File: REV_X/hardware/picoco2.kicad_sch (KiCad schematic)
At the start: 40 parts, among them J1 Conn_01x03_Female, J2 Micro_SD_Card, J3 Conn_01x03_Female, Q1 Q_NMOS_GDS, SW1 SW_Push, SW2 SW_Push, U1 PicoW, U2 scd30, U3 ssd1306, U4 PCF8523T, U5 MCP73831-2-OT, Y1 32KHz

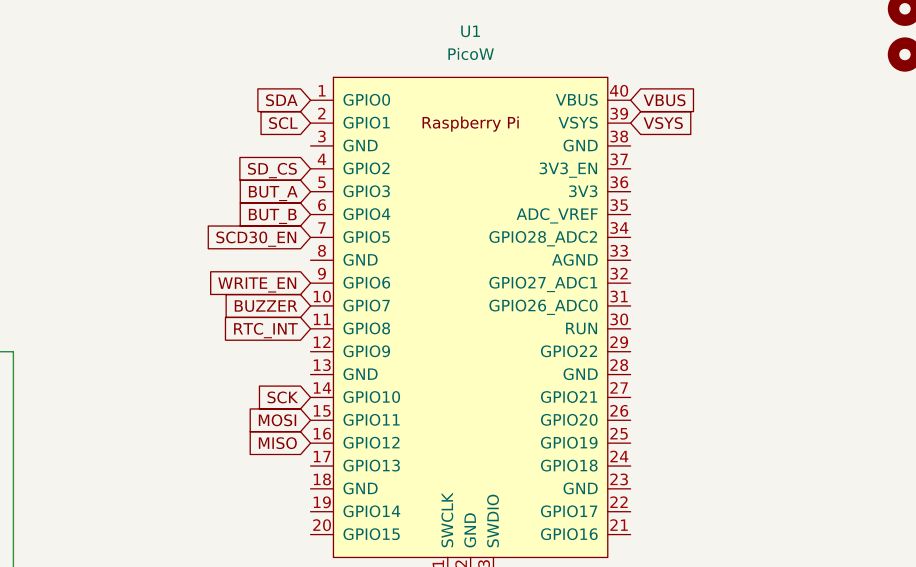
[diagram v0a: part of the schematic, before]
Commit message: add pico 3V3 and GND
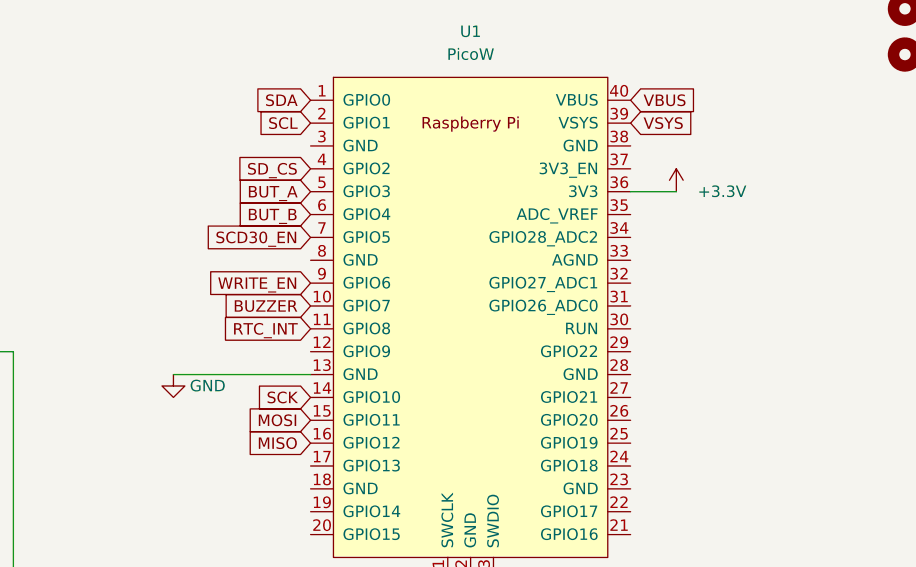
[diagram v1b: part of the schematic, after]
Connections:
- net +3V3: now also U1.36 (3V3)
- net GND: now also U1.13 (GND)
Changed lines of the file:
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@@
+    (stroke (width 0) (type default) (color 0 0 0 0))
+  )
+  (wire (pts (xy 236.22 45.72) (xy 241.3 45.72))
     (stroke (width 0) (type default) (color 0 0 0 0))
   )
@@
   )
   (wire (pts (xy 39.37 35.56) (xy 48.26 35.56))
+    (stroke (width 0) (type default) (color 0 0 0 0))
+  )
+  (wire (pts (xy 185.42 66.04) (xy 200.66 66.04))
     (stroke (width 0) (type default) (color 0 0 0 0))
   )
@@
     )
   )
+  (symbol (lib_id "power:+3.3V") (at 241.3 45.72 0) (unit 1)
+    (in_bom yes) (on_board yes)
+    (property "Reference" "#PWR0126" (id 0) (at 241.3 49.53 0)
+      (effects (font (size 1.27 1.27)) hide)
+    )
+    (property "Value" "+3.3V" (id 1) (at 246.38 45.72 0))
+    (property "Footprint" "" (id 2) (at 241.3 45.72 0)
+      (effects (font (size 1.27 1.27)) hide)
+    )
+    (property "Datasheet" "" (id 3) (at 241.3 45.72 0)
+      (effects (font (size 1.27 1.27)) hide)
+    )
+    (pin "1")
+  )
   (symbol (lib_id "Device:D") (at 101.6 52.07 180) (unit 1)
     (in_bom yes) (on_board yes) (fields_autoplaced)
@@
     (pin "2")
   )
+  (symbol (lib_id "power:GND") (at 185.42 66.04 0) (unit 1)
+    (in_bom yes) (on_board yes)
+    (property "Reference" "#PWR?" (id 0) (at 185.42 72.39 0)
+      (effects (font (size 1.27 1.27)) hide)
+    )
+    (property "Value" "GND" (id 1) (at 189.23 67.31 0))
+    (property "Footprint" "" (id 2) (at 185.42 66.04 0)
+      (effects (font (size 1.27 1.27)) hide)
+    )
+    (property "Datasheet" "" (id 3) (at 185.42 66.04 0)
+      (effects (font (size 1.27 1.27)) hide)
+    )
+    (pin "1")
+  )
   (sheet_instances
     (path "/" (page "1"))
@@
       (reference "#PWR0124") (unit 1) (value "GND") (footprint "")
     )
+    (path "/8867441f-5e7e-4f76-a3ca-d8bd64395281"
+      (reference "#PWR0126") (unit 1) (value "+3.3V") (footprint "")
+    )
+    (path "/fed51e1e-0b7c-4677-aacc-4e63d69ab5d1"
+      (reference "#PWR?") (unit 1) (value "GND") (footprint "")
+    )
     (path "/223af7cc-a0d5-4e22-9574-6b9ea27ce9a0"
